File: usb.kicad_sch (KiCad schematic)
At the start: 14 parts, among them J1 GT-USB-7010ASV, Q1 S8050, Q2 S8050, U1 CP2104

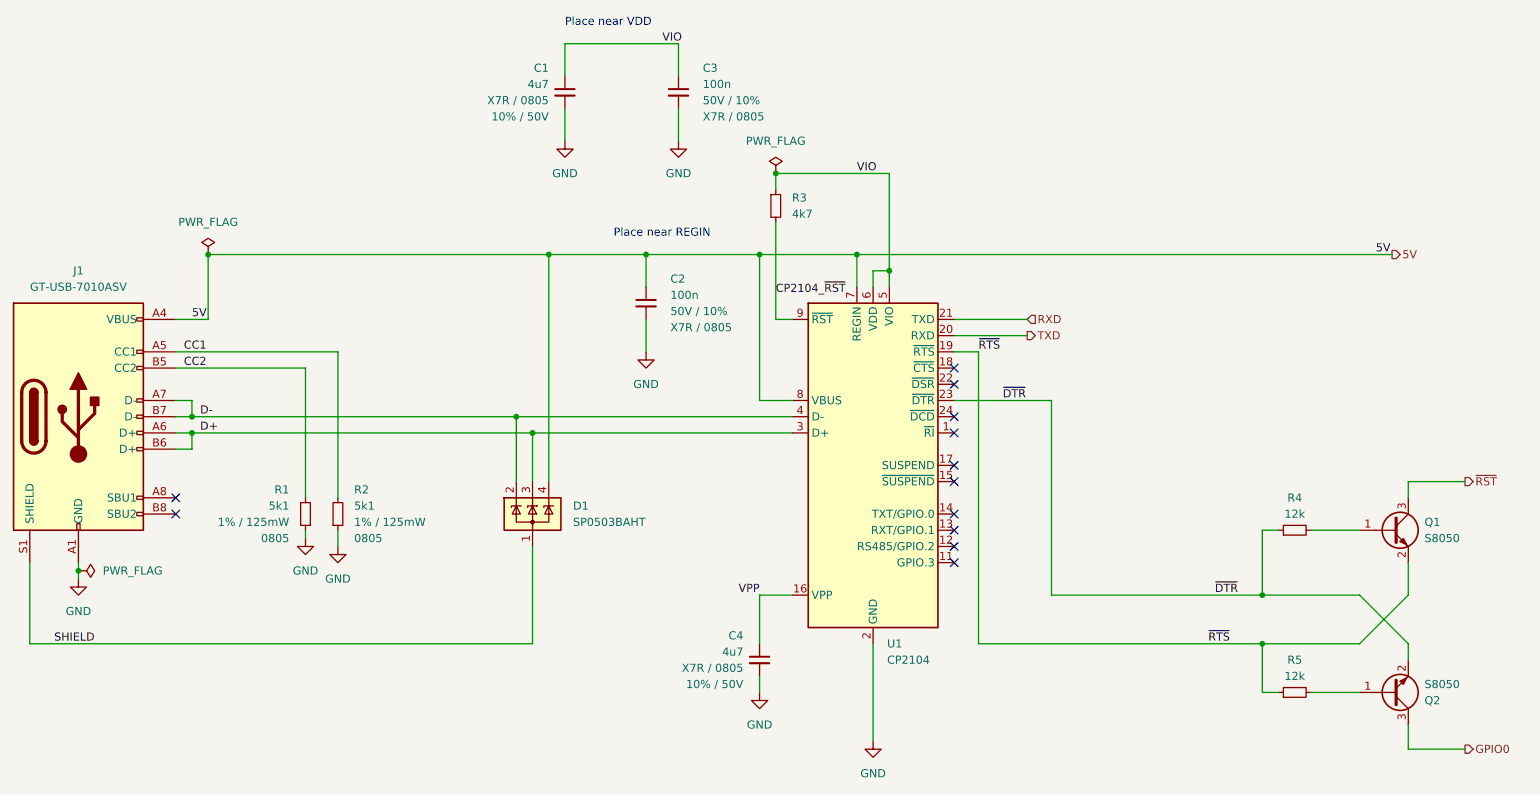
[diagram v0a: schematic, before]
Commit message: Switch to ESP32
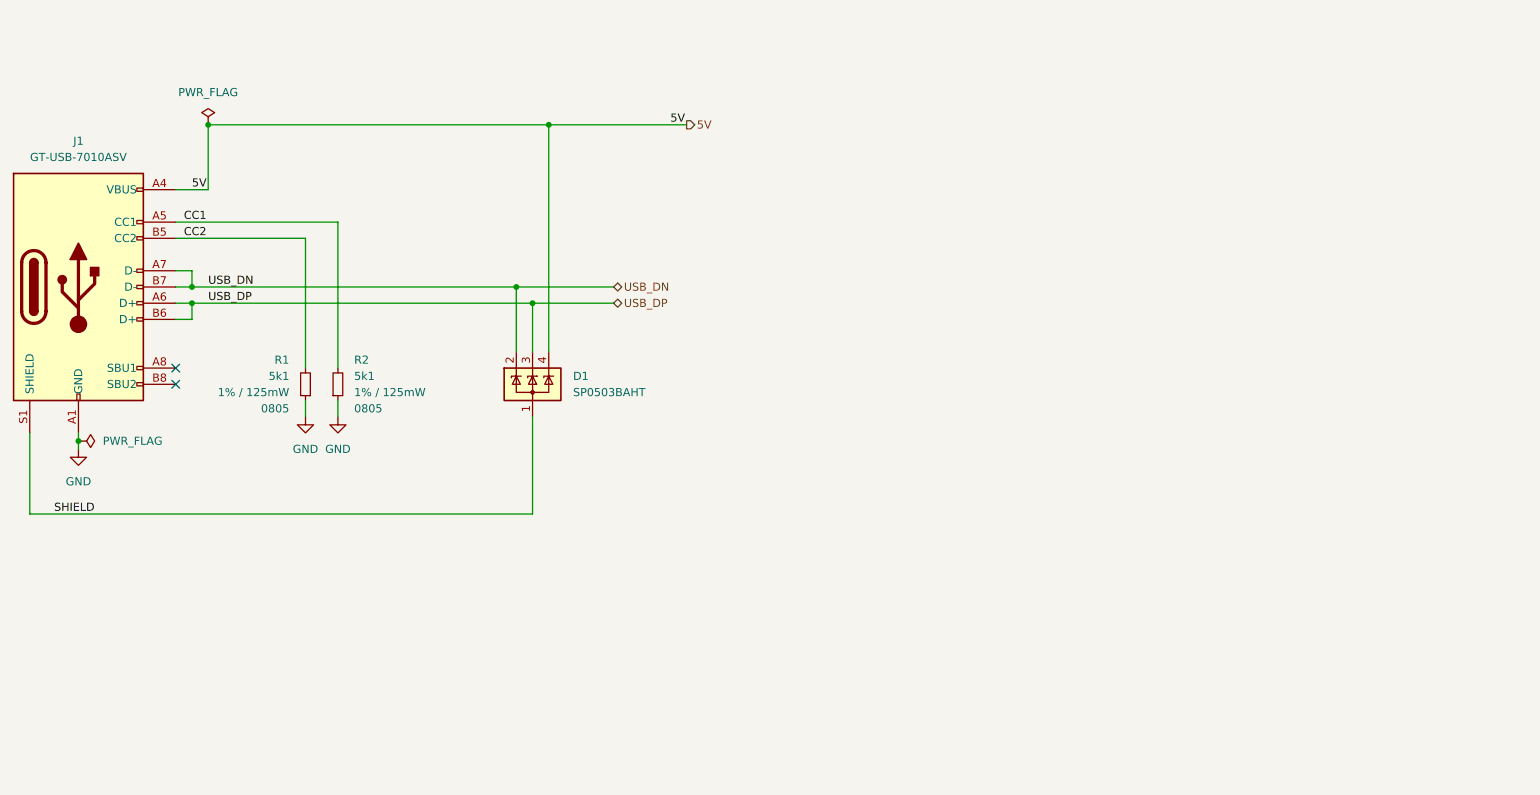
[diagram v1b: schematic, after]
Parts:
- removed C1, C4: 4u7, Capacitor_SMD:C_0805_2012Metric, symbol Device:C_Small
- removed C2, C3: 100n, Capacitor_SMD:C_0805_2012Metric, symbol Device:C_Small
- removed Q1, Q2: S8050, Package_TO_SOT_SMD:SOT-23-3, symbol Transistor_BJT:Q_NPN_BEC
- removed R3: 4k7, Resistor_SMD:R_0805_2012Metric, symbol Device:R_Small
- removed R4, R5: 12k, Resistor_SMD:R_0805_2012Metric, symbol Device:R_Small
- removed U1: CP2104, Package_DFN_QFN:QFN-24-1EP_4x4mm_P0.5mm_EP2.6x2.6mm, symbol Interface_USB:CP2104
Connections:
- net D+ renamed USB_DP
- net D- renamed USB_DN
- no-connect marks 12 -> 2
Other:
- note removed: "Place near REGIN"
- note removed: "Place near VDD"
- company: (none) -> Marcel Robitaille
- title: (none) -> USB
- moved on the sheet: D1, J1, R1, R2
